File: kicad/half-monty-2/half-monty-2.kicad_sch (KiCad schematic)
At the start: 23 parts, among them J1 Conn_01x04_Pin, J2 Conn_01x06_Pin, J3 Conn_01x06_Pin, J4 LiPo2, SW1 Select, SW2 Go, SW3 ON-OFF, U1 DRV8833PWP, U2 AP1117-50

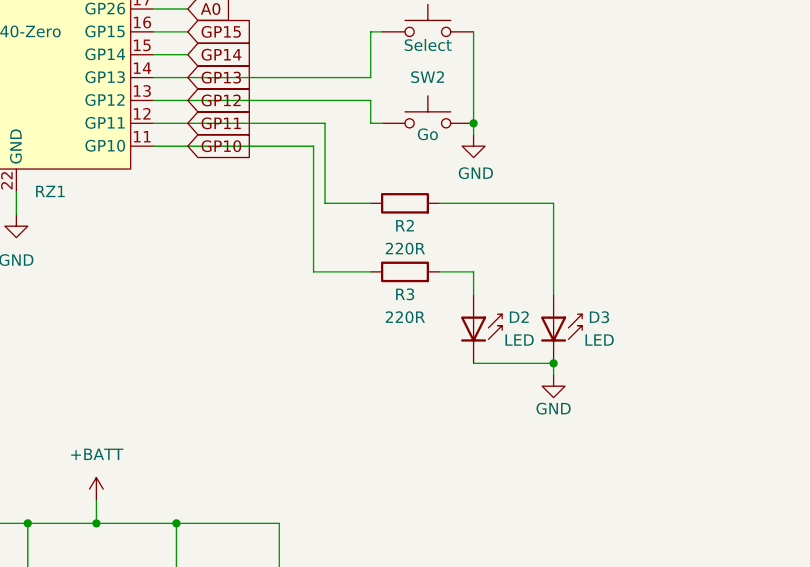
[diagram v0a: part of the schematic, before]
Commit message: Update component values after prototype assembly
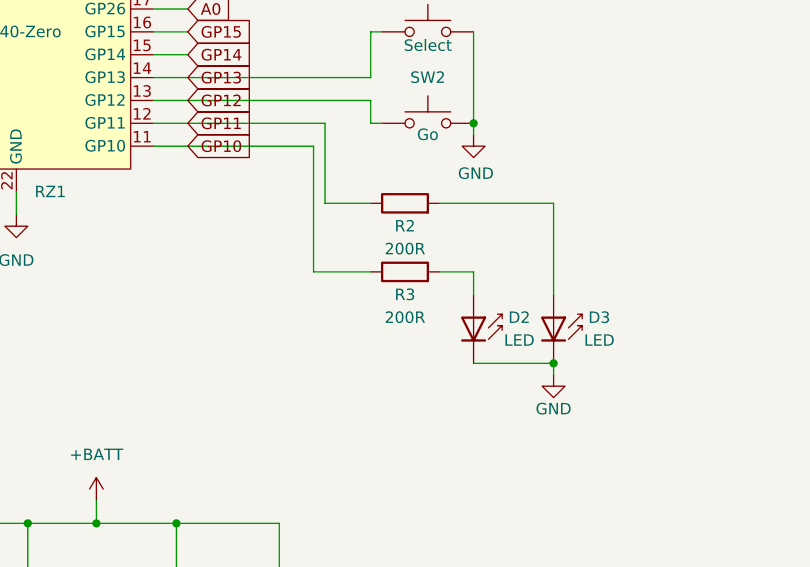
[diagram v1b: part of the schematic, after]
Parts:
- R2, R3: value 220R -> 200R
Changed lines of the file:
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@@
 			)
 		)
-		(property "Value" "220R"
+		(property "Value" "200R"
 			(at 105.41 88.9 90)
 			(effects
@@
 			)
 		)
-		(property "Value" "220R"
+		(property "Value" "200R"
 			(at 105.41 81.28 90)
 			(effects
